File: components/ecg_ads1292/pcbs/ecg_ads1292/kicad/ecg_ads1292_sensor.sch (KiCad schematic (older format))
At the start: 36 parts, among them IC1 ADS1292, U1 TPS73033DBVT

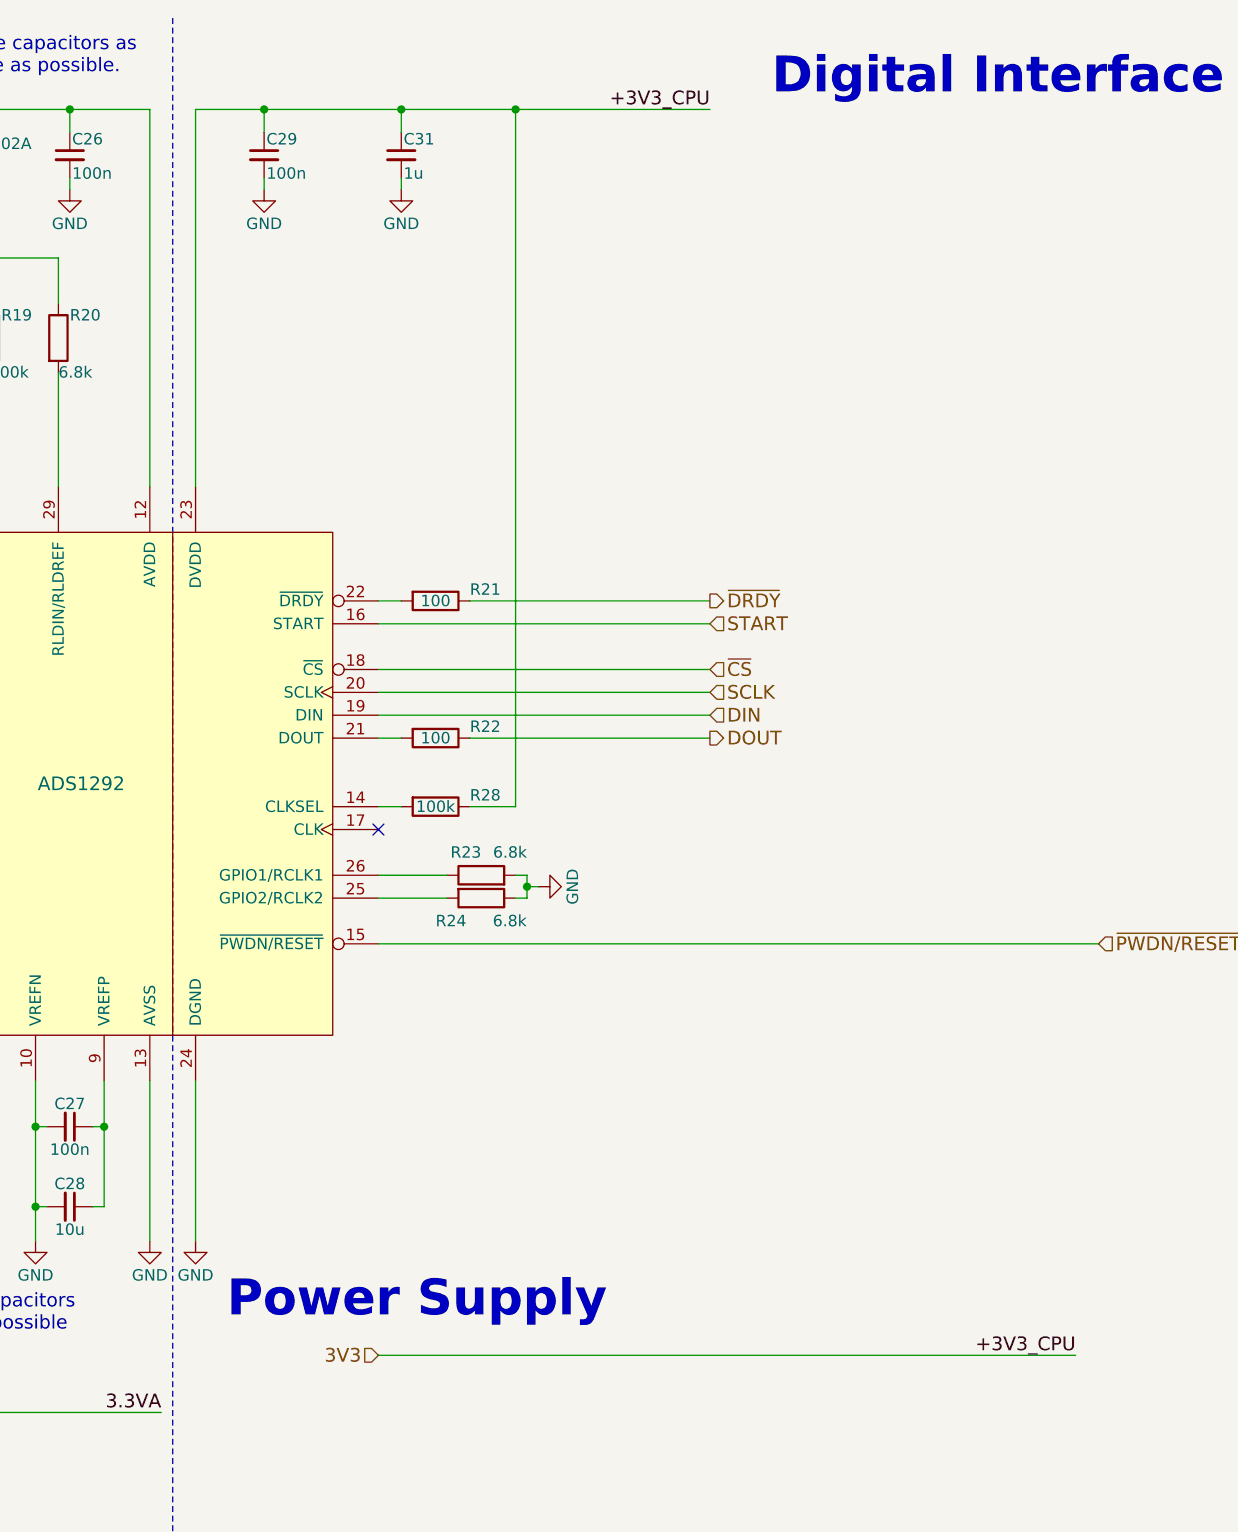
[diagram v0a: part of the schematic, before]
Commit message: simplify ads1292 supply scheme in schematic
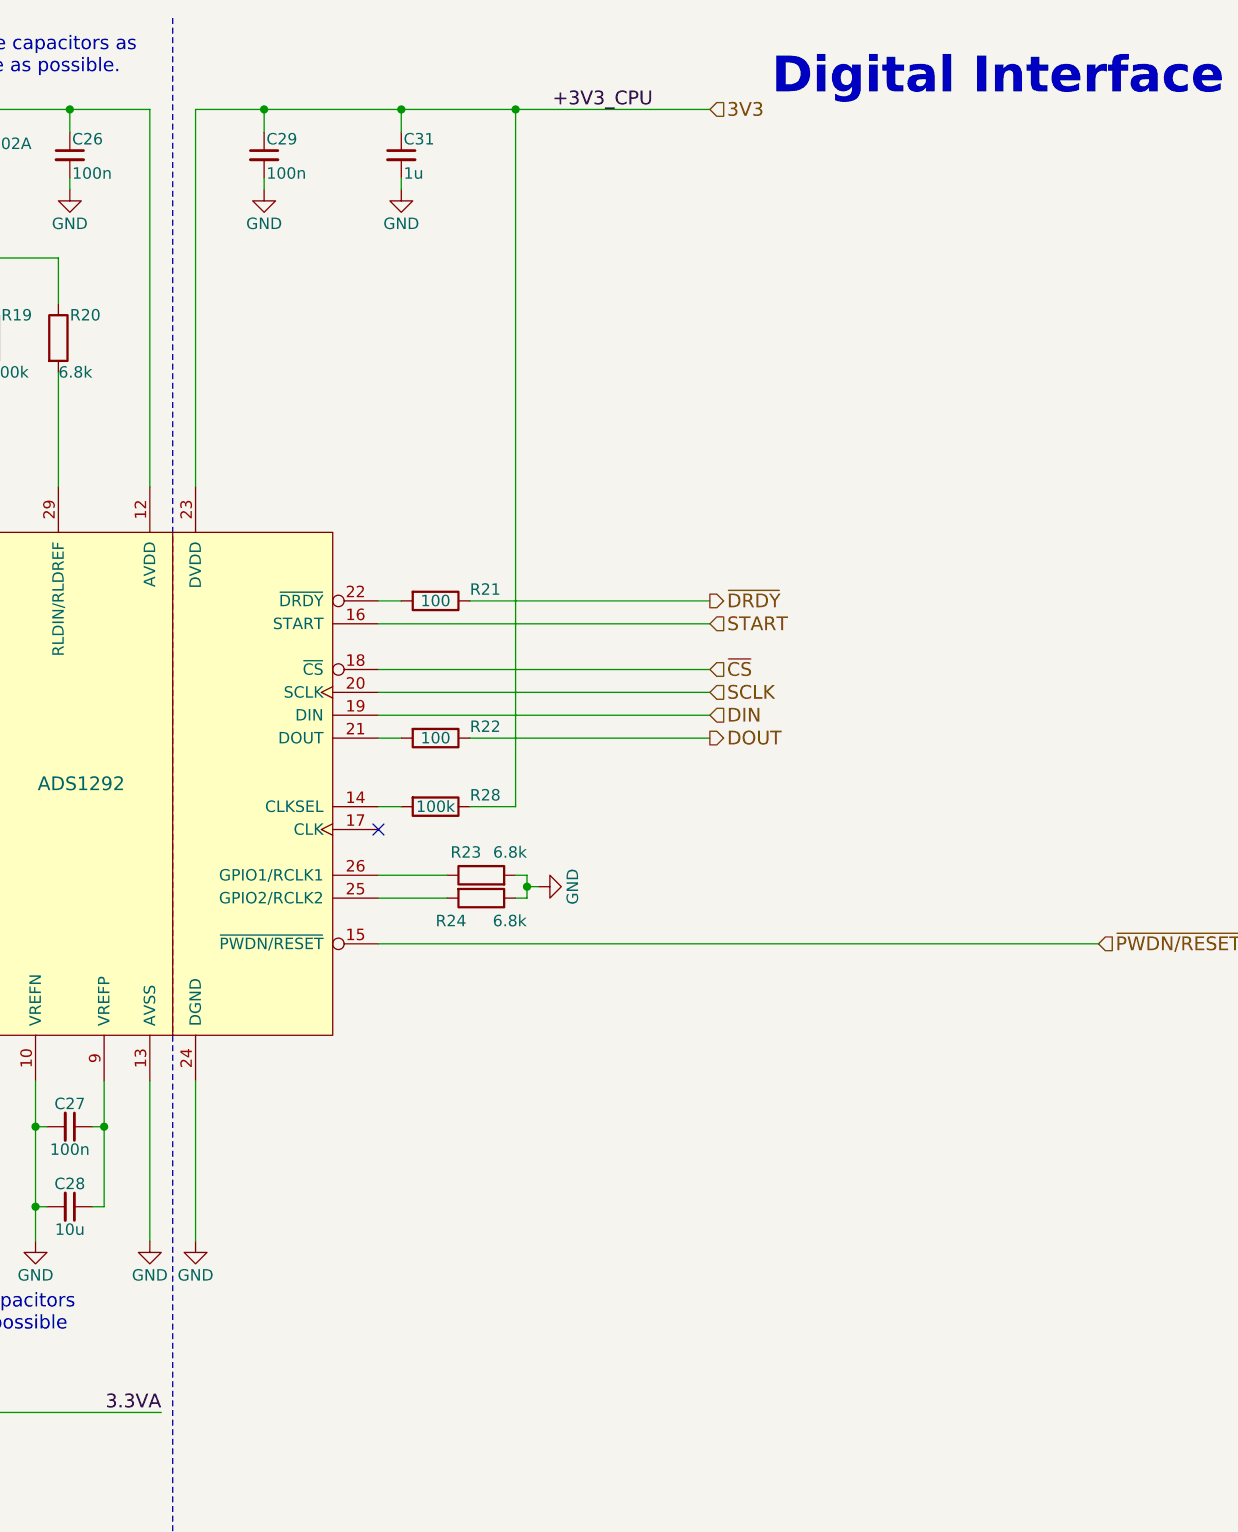
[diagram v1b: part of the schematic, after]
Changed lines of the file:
@@
 Text Notes 5000 6200 0    60   ~ 0
 place all 4 capacitors\n as close as possible\n
-Text HLabel 7200 6300 0    60   Input ~ 0
+Text HLabel 8650 850  2    60   Input ~ 0
 3V3
 Text HLabel 900  6550 0    60   Input ~ 0
@@
 Text Notes 2700 800  2    157  ~ 31
 Analog Frontend
-Text Notes 8200 6150 2    157  ~ 31
-Power Supply\n
-Text Label 8650 850  2    60   ~ 0
-+3V3_CPU
-Text Label 10250 6300 2    60   ~ 0
+Text Label 8400 850  2    60   ~ 0
 +3V3_CPU
 Text Label 4100 850  0    60   ~ 0
@@
 	6700 1150 6700 1200
 Wire Wire Line
-	10250 6300 7200 6300
-Wire Wire Line
 	4900 1500 4900 1750
